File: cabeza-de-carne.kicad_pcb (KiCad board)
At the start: 2 copper layers, 28.2 x 29.7 mm, 20 parts, among them J1 Stomp_Connector, J2 Power_Connector, Q1 2N3904, Q2 BC182L

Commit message: 0.2: more compact board
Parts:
- D1: footprint LED_THT:LED_D5.0mm -> LED_THT:LED_D3.0mm
- D2: footprint Diode_THT:D_DO-41_SOD81_P10.16mm_Horizontal -> diodes:DO41-2
- moved C4 17.7 mm to (242.2, -33.8), turned to 180 degrees
- moved R1 14.8 mm to (245.8, -37.7), turned to -90 degrees
- moved C1 10.8 mm to (237.2, -36.8), turned to 0 degrees
- moved R7 7.92 mm to (234.9, -33.2)
- moved R4 6.26 mm to (236.1, -43.4)
- moved R2 6.26 mm to (243.7, -40.3)
- moved D2 6.12 mm to (248.7, -42.7)
- moved C6 5.36 mm to (243.8, -47.3), turned to 0 degrees
- moved Q2 4.38 mm to (232.6, -41.0), turned to -90 degrees
- moved C3 4.00 mm to (235.2, -49.4)
- moved C5 3.79 mm to (230.0, -48.0)
- moved R5 2.86 mm to (226.8, -52.5)
- moved R6 2.84 mm to (248.8, -30.1)
- moved R3 2.80 mm to (244.2, -52.5)
- moved Q1 2.75 mm to (228.0, -41.0), turned to -90 degrees
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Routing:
- net Net-(C2-Pad2): track 12.2 -> 27.1 mm
- net Net-(C5-Pad1): track 28.3 -> 36.7 mm
- net IN: track 6.06 -> 12.8 mm
- net +9V: track 4.18 -> 10.3 mm
- net Net-(C6-Pad1): track 27.8 -> 21.8 mm
- net Net-(C3-Pad2): track 27.2 -> 21.9 mm
- net Net-(C4-Pad1): track 16.6 -> 13.0 mm
- net Net-(C4-Pad2): track 3.51 -> 6.18 mm
- net Net-(D1-Pad2): track 5.55 -> 3.50 mm
- net Net-(C1-Pad2): track 26.5 -> 25.2 mm
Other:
- board size 28.2 x 29.7 mm -> 25.7 x 29.8 mm
- board text added: "v0.2 2020-03-13"
- board text removed: "v0.1 2020-03-12"

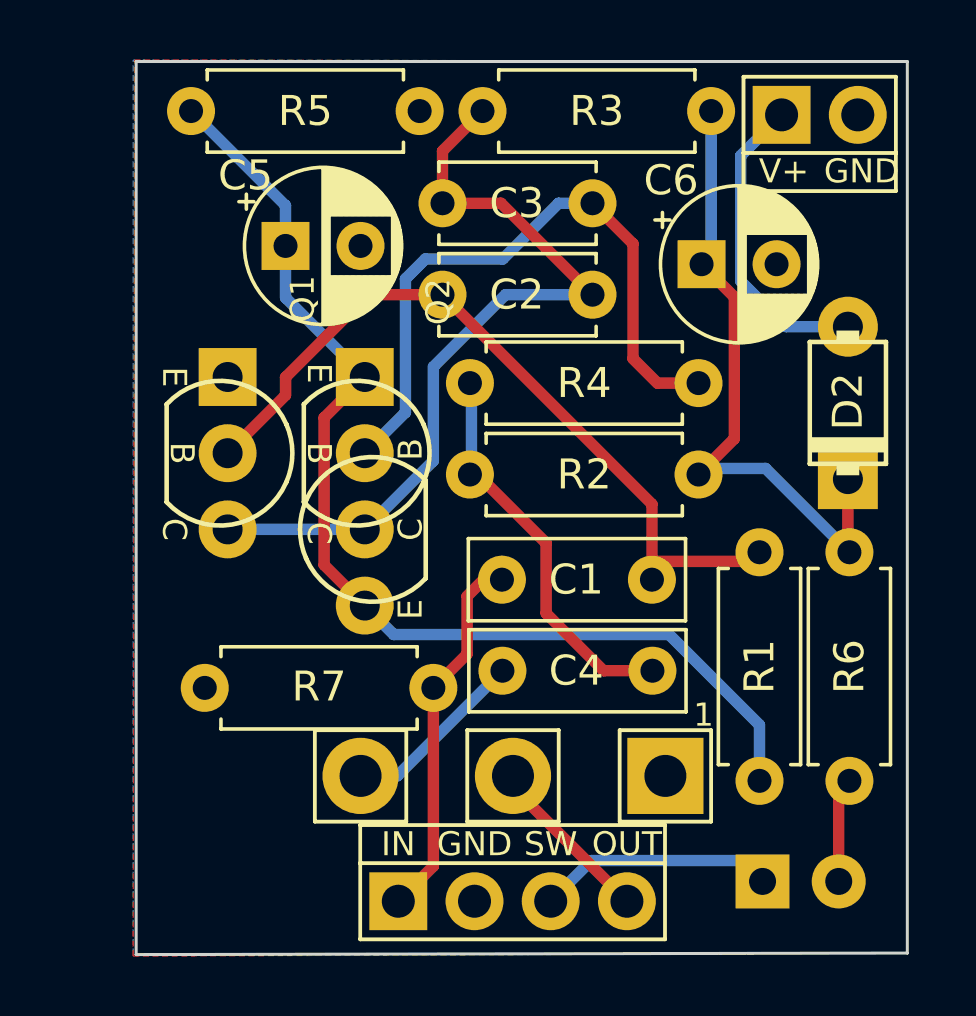
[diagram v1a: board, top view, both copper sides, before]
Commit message: v0.3: longer footprint for D1 (not standing anymore), fixed silkscreen for Q2 (had wrong markings for B,C)
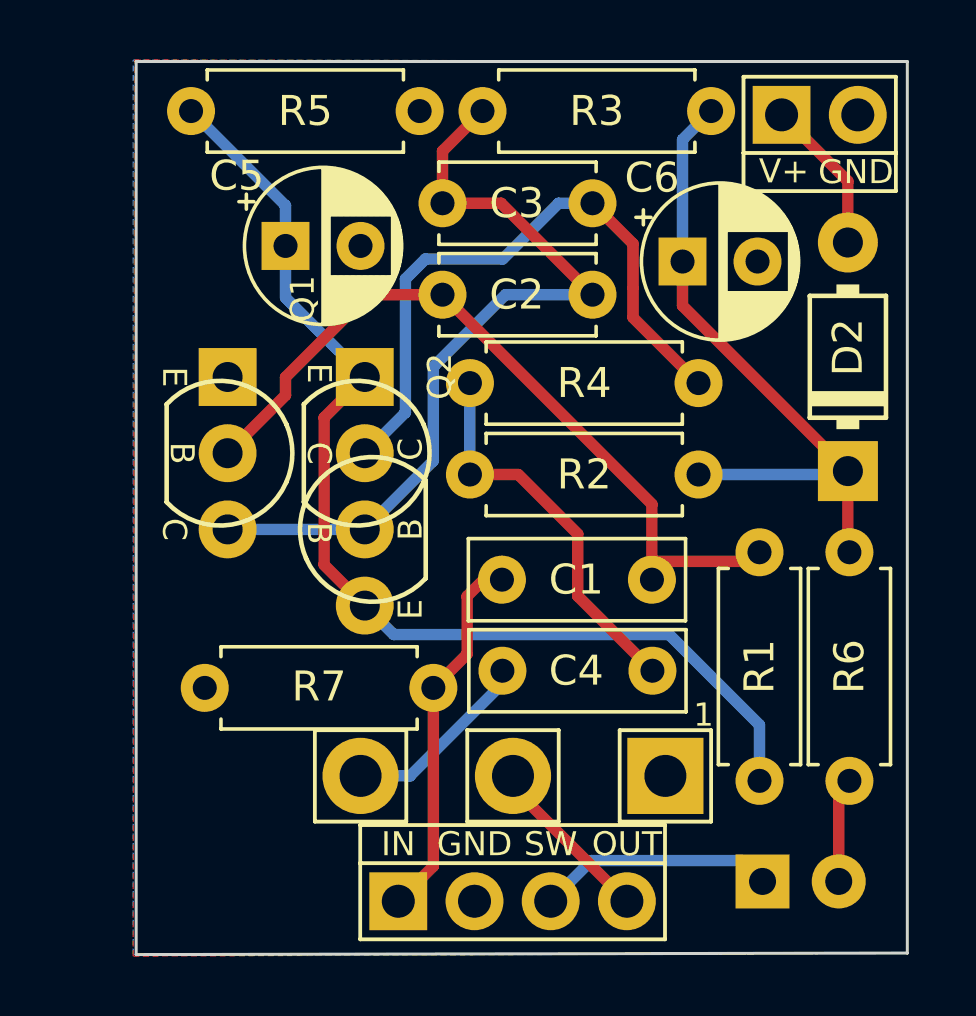
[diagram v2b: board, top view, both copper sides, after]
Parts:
- D2: footprint diodes:DO41-2 -> diodes:DO41-3
- Q2: footprint rockola_kicad_footprints:TO92_EBCE -> rockola_kicad_footprints:TO92_ECBE
- moved D2 1.54 mm to (248.7, -44.3)
- moved C6 0.64 mm to (243.2, -47.4)
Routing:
- net +9V: track 10.3 -> 5.17 mm
- net Net-(C3-Pad2): track 21.9 -> 21.1 mm
- net Net-(C6-Pad1): track 21.8 -> 22.4 mm
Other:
- board text added: "v0.3 2020-04-12"
- board text removed: "v0.2 2020-03-13"

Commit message: v0.3 gerbers, images
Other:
- board size 25.7 x 29.8 mm -> 25.7 x 29.6 mm
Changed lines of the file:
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@@
   (page "A4")
   (layers
-    (0 "F.Cu" signal)
-    (31 "B.Cu" signal)
+    (0 "F.Cu" signal hide)
+    (31 "B.Cu" signal hide)
     (32 "B.Adhes" user)
     (33 "F.Adhes" user)
@@
     (47 "F.CrtYd" user)
     (48 "B.Fab" user)
-    (49 "F.Fab" user)
+    (49 "F.Fab" user hide)
   )
   (setup
@@
       (dielectric_constraints no)
     )
-    (last_trace_width 0.381)
+    (last_trace_width 0.25)
     (user_trace_width 0.254)
     (user_trace_width 0.381)
@@
     (effects (font (size 1.1 0.95) (thickness 0.15)) (justify mirror))
   )
-  (gr_line (start 250.698 -54.102) (end 250.698 -24.384) (layer "Edge.Cuts") (width 0.1))
+  (gr_line (start 250.698 -54.102) (end 250.698 -24.511) (layer "Edge.Cuts") (width 0.1))
   (gr_line (start 224.9932 -54.102) (end 250.698 -54.102) (layer "Edge.Cuts") (width 0.1))
-  (gr_line (start 224.9932 -24.3332) (end 224.9932 -54.102) (layer "Edge.Cuts") (width 0.1))
-  (gr_line (start 250.698 -24.384) (end 224.9932 -24.3332) (layer "Edge.Cuts") (width 0.1))
+  (gr_line (start 224.9932 -24.511) (end 224.9932 -54.102) (layer "Edge.Cuts") (width 0.1))
+  (gr_line (start 250.698 -24.511) (end 224.9932 -24.511) (layer "Edge.Cuts") (width 0.1))
   (segment (start 232.473501 -30.289499) (end 234.124499 -30.289499) (width 0.381) (layer "B.Cu") (net 5))
   (segment (start 234.124499 -30.289499) (end 237.2017 -33.3667) (width 0.381) (layer "B.Cu") (net 5))

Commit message: updated to KiCad 6.0
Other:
- net class Default removed
- rule pad_to_mask_clearance: 0.051 -> 0
